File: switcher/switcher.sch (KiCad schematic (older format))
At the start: 61 parts, among them J1 DCDC, J10 GP3, J11 I1, J12 I2, J13 I3, J14 Barrel_Jack_Switch, J2 USB_B_Micro, J3 Power, J4 UART, J5 O1, J6 O2, J7 O3, J8 GP1, J9 GP2, Q1 BC549, Q2 BC549, Q3 BC549, Q4 BC549, Q5 BC549, Q8 BC549, U1 ESP-12E

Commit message: finish the switcher pcb
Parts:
- removed J4: UART, Connector_PinHeader_2.54mm:PinHeader_1x04_P2.54mm_Vertical, symbol Connector_Generic:Conn_01x04
- removed JP1, JP3, JP5: USE_3v3, Connector_PinHeader_2.54mm:PinHeader_1x02_P2.54mm_Vertical, symbol Device:Jumper
- removed JP2, JP4, JP6: USE_VDD, Connector_PinHeader_2.54mm:PinHeader_1x02_P2.54mm_Vertical, symbol Device:Jumper
- removed Q1, Q2, Q3, Q4, Q5, Q8: BC549, Package_TO_SOT_THT:TO-92, symbol Transistor_BJT:BC549
- added J16, J4: POWER_OUT, Connector_PinHeader_2.54mm:PinHeader_1x03_P2.54mm_Vertical, symbol Connector_Generic:Conn_01x03
- added J17: DEBUG, Connector_PinHeader_2.54mm:PinHeader_1x06_P2.54mm_Vertical, symbol Connector_Generic:Conn_01x06
- added JP1, JP2, JP3: VSEL, Connector_PinHeader_2.54mm:PinHeader_2x02_P2.54mm_Vertical, symbol jumpers:Jumper_Dual
- added Q1, Q2, Q3, Q4, Q5, Q6: BC817, Package_TO_SOT_SMD:SOT-23, symbol Transistor_BJT:BC817
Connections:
- wire segments 184 -> 192
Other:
- moved on the sheet: R10, R23

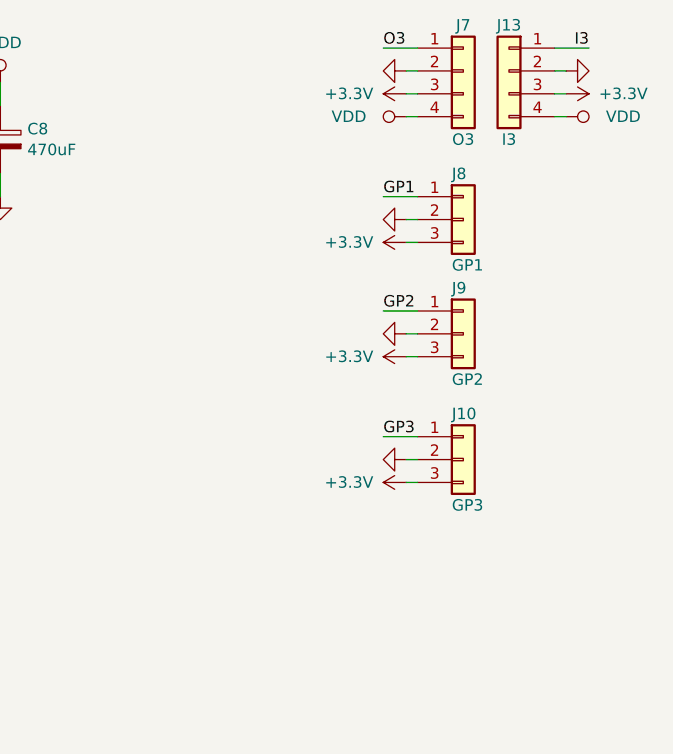
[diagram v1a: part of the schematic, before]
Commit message: driver_motor library and some changes to switcher
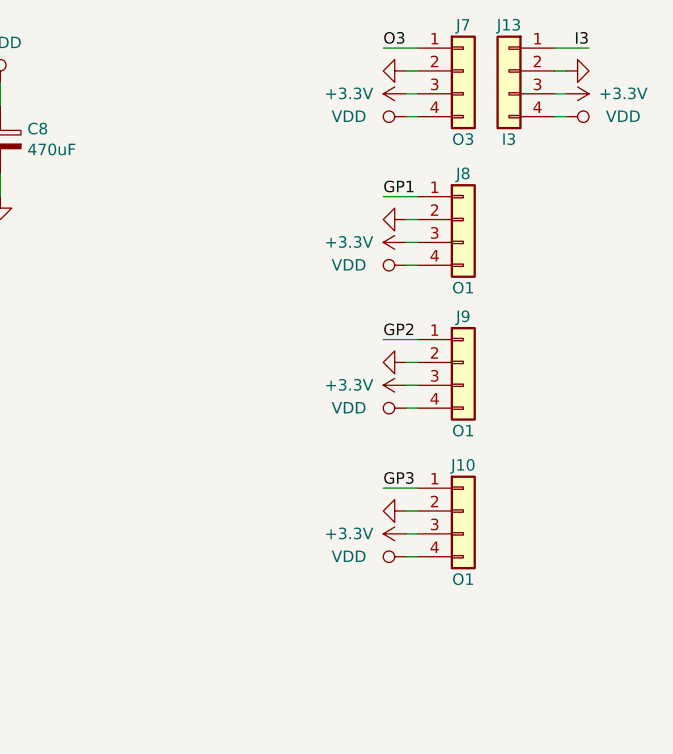
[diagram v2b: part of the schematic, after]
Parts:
- removed J10: GP3, Connector_PinHeader_2.54mm:PinHeader_1x03_P2.54mm_Vertical, symbol Connector_Generic:Conn_01x03
- removed J8: GP1, Connector_PinHeader_2.54mm:PinHeader_1x03_P2.54mm_Vertical, symbol Connector_Generic:Conn_01x03
- removed J9: GP2, Connector_PinHeader_2.54mm:PinHeader_1x03_P2.54mm_Vertical, symbol Connector_Generic:Conn_01x03
- added J10, J8, J9: O1, Connector_PinHeader_2.54mm:PinHeader_1x04_P2.54mm_Vertical, symbol Connector_Generic:Conn_01x04
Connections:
- net +3V3: now also J10.3 (Pin_3), J8.3 (Pin_3), J9.3 (Pin_3)
- net GND: now also J10.2 (Pin_2), J8.2 (Pin_2), J9.2 (Pin_2)
- net GP1: now also J8.1 (Pin_1)
- net GP2: now also J9.1 (Pin_1)
- net GP3: now also J10.1 (Pin_1)
- net VDD: now also J10.4 (Pin_4), J8.4 (Pin_4), J9.4 (Pin_4)
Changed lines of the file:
@@
 EESchema Schematic File Version 5
-EELAYER 32 0
+EELAYER 33 0
 EELAYER END
 $Descr A3 16535 11693
@@
 	13100 6600 13250 6600
 Wire Wire Line
-	13100 7100 13250 7100
-Wire Wire Line
-	13100 7650 13250 7650
+	13100 7225 13250 7225
+Wire Wire Line
+	13100 7875 13250 7875
 Wire Wire Line
 	13175 3700 13250 3700
@@
 	13200 6700 13250 6700
 Wire Wire Line
-	13200 7200 13250 7200
-Wire Wire Line
-	13200 7750 13250 7750
+	13200 6900 13250 6900
+Wire Wire Line
+	13200 7325 13250 7325
+Wire Wire Line
+	13200 7525 13250 7525
+Wire Wire Line
+	13200 7975 13250 7975
+Wire Wire Line
+	13200 8175 13250 8175
 Wire Wire Line
 	13250 4000 12800 4000
@@
 	13250 6800 13200 6800
 Wire Wire Line
-	13250 7300 13200 7300
-Wire Wire Line
-	13250 7850 13200 7850
+	13250 7425 13200 7425
+Wire Wire Line
+	13250 8075 13200 8075
 Wire Wire Line
 	13900 4750 13850 4750
@@
 Text Label 13100 6600 0    50   ~ 0
 GP1
-Text Label 13100 7100 0    50   ~ 0
+Text Label 13100 7225 0    50   ~ 0
 GP2
-Text Label 13100 7650 0    50   ~ 0
+Text Label 13100 7875 0    50   ~ 0
 GP3
 Text Label 14000 4650 2    50   ~ 0
@@
 $EndComp
 $Comp
+L power:VDD #PWR0157
+U 1 1 5E84CDAD
+P 13200 6900
+F 0 "#PWR0157" H 13200 6750 50  0001 C CNN
+F 1 "VDD" V 13200 7150 50  0000 C CNN
+F 2 "" H 13200 6900 50  0001 C CNN
+F 3 "" H 13200 6900 50  0001 C CNN
+	1    13200 6900
+	0    -1   -1   0
+$EndComp
+$Comp
 L power:+3.3V #PWR0145
 U 1 1 5DD7AFF3
-P 13200 7300
-F 0 "#PWR0145" H 13200 7150 50  0001 C CNN
-F 1 "+3.3V" V 13200 7550 50  0000 C CNN
-F 2 "" H 13200 7300 50  0001 C CNN
-F 3 "" H 13200 7300 50  0001 C CNN
-	1    13200 7300
+P 13200 7425
+F 0 "#PWR0145" H 13200 7275 50  0001 C CNN
+F 1 "+3.3V" V 13200 7675 50  0000 C CNN
+F 2 "" H 13200 7425 50  0001 C CNN
+F 3 "" H 13200 7425 50  0001 C CNN
+	1    13200 7425
+	0    -1   -1   0
+$EndComp
+$Comp
+L power:VDD #PWR0160
+U 1 1 5E84E4EF
+P 13200 7525
+F 0 "#PWR0160" H 13200 7375 50  0001 C CNN
+F 1 "VDD" V 13200 7775 50  0000 C CNN
+F 2 "" H 13200 7525 50  0001 C CNN
+F 3 "" H 13200 7525 50  0001 C CNN
+	1    13200 7525
 	0    -1   -1   0
 $EndComp
@@
 L power:+3.3V #PWR0147
 U 1 1 5DD7C022
-P 13200 7850
-F 0 "#PWR0147" H 13200 7700 50  0001 C CNN
-F 1 "+3.3V" V 13200 8100 50  0000 C CNN
-F 2 "" H 13200 7850 50  0001 C CNN
-F 3 "" H 13200 7850 50  0001 C CNN
-	1    13200 7850
+P 13200 8075
+F 0 "#PWR0147" H 13200 7925 50  0001 C CNN
+F 1 "+3.3V" V 13200 8325 50  0000 C CNN
+F 2 "" H 13200 8075 50  0001 C CNN
+F 3 "" H 13200 8075 50  0001 C CNN
+	1    13200 8075
+	0    -1   -1   0
+$EndComp
+$Comp
+L power:VDD #PWR0163
+U 1 1 5E84F9ED
+P 13200 8175
+F 0 "#PWR0163" H 13200 8025 50  0001 C CNN
+F 1 "VDD" V 13200 8425 50  0000 C CNN
+F 2 "" H 13200 8175 50  0001 C CNN
+F 3 "" H 13200 8175 50  0001 C CNN
+	1    13200 8175
 	0    -1   -1   0
 $EndComp
@@
 L power:GND #PWR0146
 U 1 1 5DD7B001
-P 13200 7200
-F 0 "#PWR0146" H 13200 6950 50  0001 C CNN
-F 1 "GND" H 13204 7045 50  0001 C CNN
-F 2 "" H 13200 7200 50  0001 C CNN
-F 3 "" H 13200 7200 50  0001 C CNN
-	1    13200 7200
+P 13200 7325
+F 0 "#PWR0146" H 13200 7075 50  0001 C CNN
+F 1 "GND" H 13204 7170 50  0001 C CNN
+F 2 "" H 13200 7325 50  0001 C CNN
+F 3 "" H 13200 7325 50  0001 C CNN
+	1    13200 7325
 	0    1    1    0
 $EndComp
@@
 L power:GND #PWR0148
 U 1 1 5DD7C02F
-P 13200 7750
-F 0 "#PWR0148" H 13200 7500 50  0001 C CNN
-F 1 "GND" H 13204 7595 50  0001 C CNN
-F 2 "" H 13200 7750 50  0001 C CNN
-F 3 "" H 13200 7750 50  0001 C CNN
-	1    13200 7750
+P 13200 7975
+F 0 "#PWR0148" H 13200 7725 50  0001 C CNN
+F 1 "GND" H 13204 7820 50  0001 C CNN
+F 2 "" H 13200 7975 50  0001 C CNN
+F 3 "" H 13200 7975 50  0001 C CNN
+	1    13200 7975
 	0    1    1    0
 $EndComp
@@
 $EndComp
 $Comp
-L Connector_Generic:Conn_01x03 J8
-U 1 1 5DD78BC0
-P 13450 6700
-F 0 "J8" H 13400 6900 50  0000 L CNN
-F 1 "GP1" H 13400 6500 50  0000 L CNN
-F 2 "Connector_PinHeader_2.54mm:PinHeader_1x03_P2.54mm_Vertical" H 13450 6700 50  0001 C CNN
-F 3 "~" H 13450 6700 50  0001 C CNN
-	1    13450 6700
-	1    0    0    -1
-$EndComp
-$Comp
-L Connector_Generic:Conn_01x03 J9
-U 1 1 5DD7AFE6
-P 13450 7200
-F 0 "J9" H 13400 7400 50  0000 L CNN
-F 1 "GP2" H 13400 7000 50  0000 L CNN
-F 2 "Connector_PinHeader_2.54mm:PinHeader_1x03_P2.54mm_Vertical" H 13450 7200 50  0001 C CNN
-F 3 "~" H 13450 7200 50  0001 C CNN
-	1    13450 7200
-	1    0    0    -1
-$EndComp
-$Comp
-L Connector_Generic:Conn_01x03 J10
-U 1 1 5DD7C03E
-P 13450 7750
-F 0 "J10" H 13400 7950 50  0000 L CNN
-F 1 "GP3" H 13400 7550 50  0000 L CNN
-F 2 "Connector_PinHeader_2.54mm:PinHeader_1x03_P2.54mm_Vertical" H 13450 7750 50  0001 C CNN
-F 3 "~" H 13450 7750 50  0001 C CNN
-	1    13450 7750
-	1    0    0    -1
-$EndComp
-$Comp
 L Connector_Generic:Conn_01x04 J1
 U 1 1 5D89C1F7
@@
 	1    0    0    -1
 $EndComp
+$Comp
+L Connector_Generic:Conn_01x04 J8
+U 1 1 5E8478BC
+P 13450 6700
+F 0 "J8" H 13450 6900 50  0000 C CNN
+F 1 "O1" H 13450 6400 50  0000 C CNN
+F 2 "Connector_PinHeader_2.54mm:PinHeader_1x04_P2.54mm_Vertical" H 13450 6700 50  0001 C CNN
+F 3 "~" H 13450 6700 50  0001 C CNN
+	1    13450 6700
+	1    0    0    -1
+$EndComp
+$Comp
+L Connector_Generic:Conn_01x04 J9
+U 1 1 5E84830F
+P 13450 7325
+F 0 "J9" H 13450 7525 50  0000 C CNN
+F 1 "O1" H 13450 7025 50  0000 C CNN
+F 2 "Connector_PinHeader_2.54mm:PinHeader_1x04_P2.54mm_Vertical" H 13450 7325 50  0001 C CNN
+F 3 "~" H 13450 7325 50  0001 C CNN
+	1    13450 7325
+	1    0    0    -1
+$EndComp
+$Comp
+L Connector_Generic:Conn_01x04 J10
+U 1 1 5E8487C4
+P 13450 7975
+F 0 "J10" H 13450 8175 50  0000 C CNN
+F 1 "O1" H 13450 7675 50  0000 C CNN
+F 2 "Connector_PinHeader_2.54mm:PinHeader_1x04_P2.54mm_Vertical" H 13450 7975 50  0001 C CNN
+F 3 "~" H 13450 7975 50  0001 C CNN
+	1    13450 7975
+	1    0    0    -1
+$EndComp

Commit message: update 0805 components to have larger pads
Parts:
- C1, C10, C2, C7: footprint Capacitor_SMD:C_0805_2012Metric -> Capacitor_SMD:C_0805_2012Metric_Pad1.15x1.40mm_HandSolder
- R10, R11, R12, R13, R14, R15, R16, R17, R18, R19, R2, R20, R21, R22, R23, R24, R25, R26, R27, R3, R4, R5, R6, R7, R8, R9: footprint Resistor_SMD:R_0805_2012Metric -> Resistor_SMD:R_0805_2012Metric_Pad1.15x1.40mm_HandSolder
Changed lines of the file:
@@
 F 0 "R2" H 4656 7646 50  0000 R CNN
 F 1 "150k" H 4656 7555 50  0000 R CNN
-F 2 "Resistor_SMD:R_0805_2012Metric" V 4655 7600 50  0001 C CNN
+F 2 "Resistor_SMD:R_0805_2012Metric_Pad1.15x1.40mm_HandSolder" V 4655 7600 50  0001 C CNN
 F 3 "~" H 4725 7600 50  0001 C CNN
 	1    4725 7600
@@
 F 0 "R3" V 5175 7000 50  0000 C CNN
 F 1 "4.7k" V 5275 7000 50  0000 C CNN
-F 2 "Resistor_SMD:R_0805_2012Metric" V 5205 7000 50  0001 C CNN
+F 2 "Resistor_SMD:R_0805_2012Metric_Pad1.15x1.40mm_HandSolder" V 5205 7000 50  0001 C CNN
 F 3 "~" H 5275 7000 50  0001 C CNN
 	1    5275 7000
@@
 F 0 "R4" V 5175 7200 50  0000 C CNN
 F 1 "4.7k" V 5275 7200 50  0000 C CNN
-F 2 "Resistor_SMD:R_0805_2012Metric" V 5205 7200 50  0001 C CNN
+F 2 "Resistor_SMD:R_0805_2012Metric_Pad1.15x1.40mm_HandSolder" V 5205 7200 50  0001 C CNN
 F 3 "~" H 5275 7200 50  0001 C CNN
 	1    5275 7200
@@
 F 0 "R6" V 5225 8100 50  0000 C CNN
 F 1 "4.7k" V 5275 8300 50  0000 C CNN
-F 2 "Resistor_SMD:R_0805_2012Metric" V 5205 8300 50  0001 C CNN
+F 2 "Resistor_SMD:R_0805_2012Metric_Pad1.15x1.40mm_HandSolder" V 5205 8300 50  0001 C CNN
 F 3 "~" H 5275 8300 50  0001 C CNN
 	1    5275 8300
@@
 F 0 "R19" V 5693 2900 50  0000 C CNN
 F 1 "1k" V 5784 2900 50  0000 C CNN
-F 2 "Resistor_SMD:R_0805_2012Metric" V 5830 2900 50  0001 C CNN
+F 2 "Resistor_SMD:R_0805_2012Metric_Pad1.15x1.40mm_HandSolder" V 5830 2900 50  0001 C CNN
 F 3 "~" H 5900 2900 50  0001 C CNN
 	1    5900 2900
@@
 F 0 "R7" V 5693 4750 50  0000 C CNN
 F 1 "1k" V 5784 4750 50  0000 C CNN
-F 2 "Resistor_SMD:R_0805_2012Metric" V 5830 4750 50  0001 C CNN
+F 2 "Resistor_SMD:R_0805_2012Metric_Pad1.15x1.40mm_HandSolder" V 5830 4750 50  0001 C CNN
 F 3 "~" H 5900 4750 50  0001 C CNN
 	1    5900 4750
@@
 F 0 "R21" H 6300 3250 50  0000 R CNN
 F 1 "4.7k" H 6350 3150 50  0000 R CNN
-F 2 "Resistor_SMD:R_0805_2012Metric" V 6080 3200 50  0001 C CNN
+F 2 "Resistor_SMD:R_0805_2012Metric_Pad1.15x1.40mm_HandSolder" V 6080 3200 50  0001 C CNN
 F 3 "~" H 6150 3200 50  0001 C CNN
 	1    6150 3200
@@
 F 0 "R8" H 6300 5100 50  0000 R CNN
 F 1 "4.7k" H 6350 5000 50  0000 R CNN
-F 2 "Resistor_SMD:R_0805_2012Metric" V 6080 5050 50  0001 C CNN
+F 2 "Resistor_SMD:R_0805_2012Metric_Pad1.15x1.40mm_HandSolder" V 6080 5050 50  0001 C CNN
 F 3 "~" H 6150 5050 50  0001 C CNN
 	1    6150 5050
@@
 F 0 "R23" H 6375 1617 50  0000 R CNN
 F 1 "1k" H 6375 1510 50  0000 R CNN
-F 2 "Resistor_SMD:R_0805_2012Metric" V 6380 1575 50  0001 C CNN
+F 2 "Resistor_SMD:R_0805_2012Metric_Pad1.15x1.40mm_HandSolder" V 6380 1575 50  0001 C CNN
 F 3 "~" H 6450 1575 50  0001 C CNN
 	1    6450 1575
@@
 F 0 "R9" H 6481 4346 50  0000 R CNN
 F 1 "1k" H 6481 4255 50  0000 R CNN
-F 2 "Resistor_SMD:R_0805_2012Metric" V 6480 4300 50  0001 C CNN
+F 2 "Resistor_SMD:R_0805_2012Metric_Pad1.15x1.40mm_HandSolder" V 6480 4300 50  0001 C CNN
 F 3 "~" H 6550 4300 50  0001 C CNN
 	1    6550 4300
@@
 F 0 "R10" H 6850 1617 50  0000 R CNN
 F 1 "4.7k" H 6875 1510 50  0000 R CNN
-F 2 "Resistor_SMD:R_0805_2012Metric" V 6580 1575 50  0001 C CNN
+F 2 "Resistor_SMD:R_0805_2012Metric_Pad1.15x1.40mm_HandSolder" V 6580 1575 50  0001 C CNN
 F 3 "~" H 6650 1575 50  0001 C CNN
 	1    6650 1575
@@
 F 0 "R5" V 6825 6400 50  0000 C CNN
 F 1 "4.7k" V 6925 6400 50  0000 C CNN
-F 2 "Resistor_SMD:R_0805_2012Metric" V 6855 6400 50  0001 C CNN
+F 2 "Resistor_SMD:R_0805_2012Metric_Pad1.15x1.40mm_HandSolder" V 6855 6400 50  0001 C CNN
 F 3 "~" H 6925 6400 50  0001 C CNN
 	1    6925 6400
@@
 F 0 "R11" V 7293 2900 50  0000 C CNN
 F 1 "1k" V 7384 2900 50  0000 C CNN
-F 2 "Resistor_SMD:R_0805_2012Metric" V 7430 2900 50  0001 C CNN
+F 2 "Resistor_SMD:R_0805_2012Metric_Pad1.15x1.40mm_HandSolder" V 7430 2900 50  0001 C CNN
 F 3 "~" H 7500 2900 50  0001 C CNN
 	1    7500 2900
@@
 F 0 "R12" V 7293 4750 50  0000 C CNN
 F 1 "1k" V 7384 4750 50  0000 C CNN
-F 2 "Resistor_SMD:R_0805_2012Metric" V 7430 4750 50  0001 C CNN
+F 2 "Resistor_SMD:R_0805_2012Metric_Pad1.15x1.40mm_HandSolder" V 7430 4750 50  0001 C CNN
 F 3 "~" H 7500 4750 50  0001 C CNN
 	1    7500 4750
@@
 F 0 "R13" H 7900 3250 50  0000 R CNN
 F 1 "4.7k" H 7950 3150 50  0000 R CNN
-F 2 "Resistor_SMD:R_0805_2012Metric" V 7680 3200 50  0001 C CNN
+F 2 "Resistor_SMD:R_0805_2012Metric_Pad1.15x1.40mm_HandSolder" V 7680 3200 50  0001 C CNN
 F 3 "~" H 7750 3200 50  0001 C CNN
 	1    7750 3200
@@
 F 0 "R14" H 7900 5100 50  0000 R CNN
 F 1 "4.7k" H 7950 5000 50  0000 R CNN
-F 2 "Resistor_SMD:R_0805_2012Metric" V 7680 5050 50  0001 C CNN
+F 2 "Resistor_SMD:R_0805_2012Metric_Pad1.15x1.40mm_HandSolder" V 7680 5050 50  0001 C CNN
 F 3 "~" H 7750 5050 50  0001 C CNN
 	1    7750 5050
@@
 F 0 "R15" H 7975 1617 50  0000 R CNN
 F 1 "1k" H 7975 1510 50  0000 R CNN
-F 2 "Resistor_SMD:R_0805_2012Metric" V 7980 1575 50  0001 C CNN
+F 2 "Resistor_SMD:R_0805_2012Metric_Pad1.15x1.40mm_HandSolder" V 7980 1575 50  0001 C CNN
 F 3 "~" H 8050 1575 50  0001 C CNN
 	1    8050 1575
@@
 F 0 "R16" H 8081 4346 50  0000 R CNN
 F 1 "1k" H 8081 4255 50  0000 R CNN
-F 2 "Resistor_SMD:R_0805_2012Metric" V 8080 4300 50  0001 C CNN
+F 2 "Resistor_SMD:R_0805_2012Metric_Pad1.15x1.40mm_HandSolder" V 8080 4300 50  0001 C CNN
 F 3 "~" H 8150 4300 50  0001 C CNN
 	1    8150 4300
@@
 F 0 "R17" H 8450 1617 50  0000 R CNN
 F 1 "4.7k" H 8475 1510 50  0000 R CNN
-F 2 "Resistor_SMD:R_0805_2012Metric" V 8180 1575 50  0001 C CNN
+F 2 "Resistor_SMD:R_0805_2012Metric_Pad1.15x1.40mm_HandSolder" V 8180 1575 50  0001 C CNN
 F 3 "~" H 8250 1575 50  0001 C CNN
 	1    8250 1575
@@
 F 0 "R18" V 8943 2900 50  0000 C CNN
 F 1 "1k" V 9034 2900 50  0000 C CNN
-F 2 "Resistor_SMD:R_0805_2012Metric" V 9080 2900 50  0001 C CNN
+F 2 "Resistor_SMD:R_0805_2012Metric_Pad1.15x1.40mm_HandSolder" V 9080 2900 50  0001 C CNN
 F 3 "~" H 9150 2900 50  0001 C CNN
 	1    9150 2900
@@
 F 0 "R20" V 8943 4750 50  0000 C CNN
 F 1 "1k" V 9034 4750 50  0000 C CNN
-F 2 "Resistor_SMD:R_0805_2012Metric" V 9080 4750 50  0001 C CNN
+F 2 "Resistor_SMD:R_0805_2012Metric_Pad1.15x1.40mm_HandSolder" V 9080 4750 50  0001 C CNN
 F 3 "~" H 9150 4750 50  0001 C CNN
 	1    9150 4750
@@
 F 0 "R22" H 9550 3250 50  0000 R CNN
 F 1 "4.7k" H 9600 3150 50  0000 R CNN
-F 2 "Resistor_SMD:R_0805_2012Metric" V 9330 3200 50  0001 C CNN
+F 2 "Resistor_SMD:R_0805_2012Metric_Pad1.15x1.40mm_HandSolder" V 9330 3200 50  0001 C CNN
 F 3 "~" H 9400 3200 50  0001 C CNN
 	1    9400 3200
@@
 F 0 "R24" H 9550 5100 50  0000 R CNN
 F 1 "4.7k" H 9600 5000 50  0000 R CNN
-F 2 "Resistor_SMD:R_0805_2012Metric" V 9330 5050 50  0001 C CNN
+F 2 "Resistor_SMD:R_0805_2012Metric_Pad1.15x1.40mm_HandSolder" V 9330 5050 50  0001 C CNN
 F 3 "~" H 9400 5050 50  0001 C CNN
 	1    9400 5050
@@
 F 0 "R25" H 9625 1617 50  0000 R CNN
 F 1 "1k" H 9625 1510 50  0000 R CNN
-F 2 "Resistor_SMD:R_0805_2012Metric" V 9630 1575 50  0001 C CNN
+F 2 "Resistor_SMD:R_0805_2012Metric_Pad1.15x1.40mm_HandSolder" V 9630 1575 50  0001 C CNN
 F 3 "~" H 9700 1575 50  0001 C CNN
 	1    9700 1575
@@
 F 0 "R26" H 9731 4346 50  0000 R CNN
 F 1 "1k" H 9731 4255 50  0000 R CNN
-F 2 "Resistor_SMD:R_0805_2012Metric" V 9730 4300 50  0001 C CNN
+F 2 "Resistor_SMD:R_0805_2012Metric_Pad1.15x1.40mm_HandSolder" V 9730 4300 50  0001 C CNN
 F 3 "~" H 9800 4300 50  0001 C CNN
 	1    9800 4300
@@
 F 0 "R27" H 10100 1617 50  0000 R CNN
 F 1 "4.7k" H 10125 1510 50  0000 R CNN
-F 2 "Resistor_SMD:R_0805_2012Metric" V 9830 1575 50  0001 C CNN
+F 2 "Resistor_SMD:R_0805_2012Metric_Pad1.15x1.40mm_HandSolder" V 9830 1575 50  0001 C CNN
 F 3 "~" H 9900 1575 50  0001 C CNN
 	1    9900 1575
@@
 F 0 "C1" H 1665 5046 50  0000 L CNN
 F 1 "100n" H 1665 4955 50  0000 L CNN
-F 2 "Capacitor_SMD:C_0805_2012Metric" H 1588 4850 50  0001 C CNN
+F 2 "Capacitor_SMD:C_0805_2012Metric_Pad1.15x1.40mm_HandSolder" H 1588 4850 50  0001 C CNN
 F 3 "~" H 1550 5000 50  0001 C CNN
 	1    1550 5000
@@
 F 0 "C2" H 4440 8196 50  0000 L CNN
 F 1 "100n" H 4440 8105 50  0000 L CNN
-F 2 "Capacitor_SMD:C_0805_2012Metric" H 4363 8000 50  0001 C CNN
+F 2 "Capacitor_SMD:C_0805_2012Metric_Pad1.15x1.40mm_HandSolder" H 4363 8000 50  0001 C CNN
 F 3 "~" H 4325 8150 50  0001 C CNN
 	1    4325 8150
@@
 F 0 "C10" H 5190 7696 50  0000 L CNN
 F 1 "10p" H 5190 7605 50  0000 L CNN
-F 2 "Capacitor_SMD:C_0805_2012Metric" H 5113 7500 50  0001 C CNN
+F 2 "Capacitor_SMD:C_0805_2012Metric_Pad1.15x1.40mm_HandSolder" H 5113 7500 50  0001 C CNN
 F 3 "~" H 5075 7650 50  0001 C CNN
 	1    5075 7650
@@
 F 0 "C7" H 11040 6396 50  0000 L CNN
 F 1 "100n" H 11040 6305 50  0000 L CNN
-F 2 "Capacitor_SMD:C_0805_2012Metric" H 10963 6200 50  0001 C CNN
+F 2 "Capacitor_SMD:C_0805_2012Metric_Pad1.15x1.40mm_HandSolder" H 10963 6200 50  0001 C CNN
 F 3 "~" H 10925 6350 50  0001 C CNN
 	1    10925 6350
